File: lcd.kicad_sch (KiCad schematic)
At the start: 11 parts, among them J2 FPC-05F-12PH20, Q1 SS8050

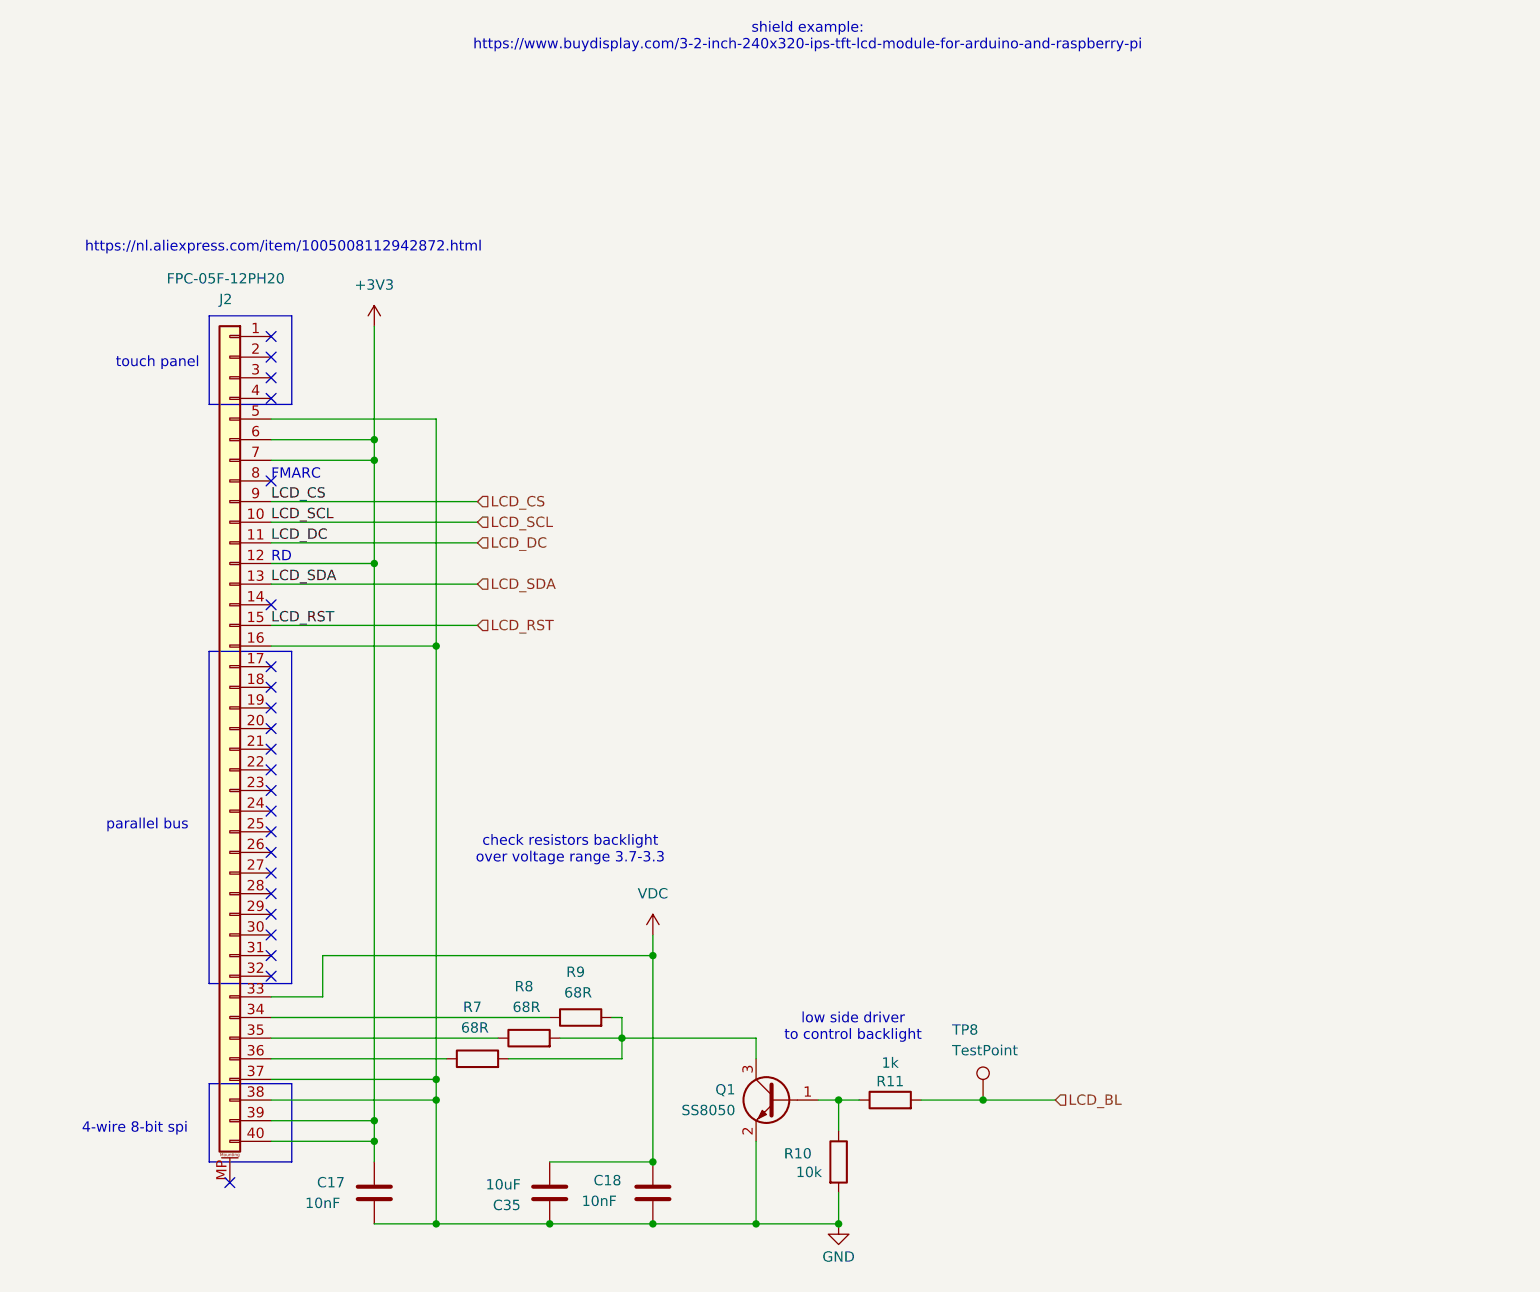
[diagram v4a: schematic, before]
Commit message: proper lcd backlight driver
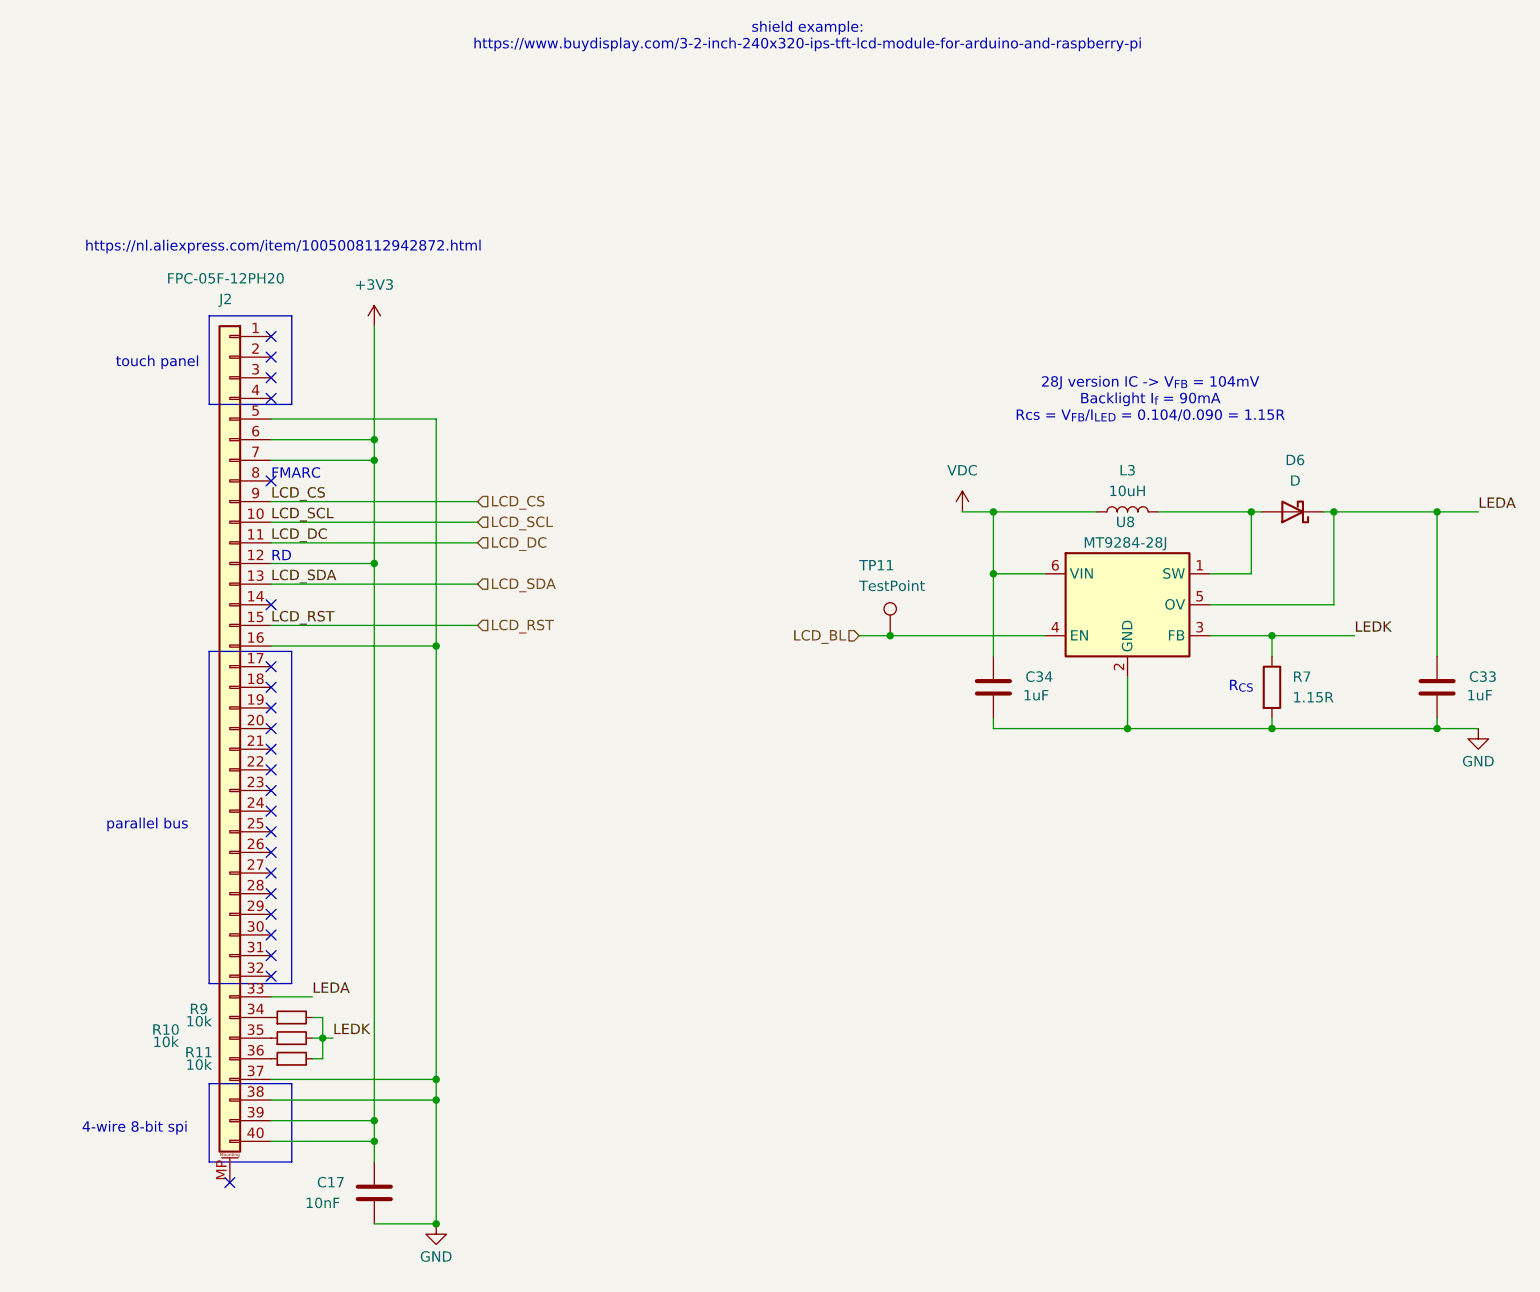
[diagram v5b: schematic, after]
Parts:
- removed C18: 10nF, Capacitor_SMD:C_0603_1608Metric, symbol Device:C
- removed C35: 10uF, Capacitor_SMD:C_0603_1608Metric, symbol Device:C
- removed Q1: SS8050, Package_TO_SOT_SMD:SOT-23, symbol Transistor_BJT:SS8050
- removed R10: 10k, Resistor_SMD:R_0603_1608Metric, symbol Device:R
- removed R11: 1k, Resistor_SMD:R_0402_1005Metric, symbol Device:R
- removed R8, R9: 68R, Resistor_SMD:R_0603_1608Metric, symbol Device:R
- removed TP8: TestPoint, TestPoint:TestPoint_Pad_D1.0mm, symbol Connector:TestPoint
- added C33, C34: 1uF, Capacitor_SMD:C_0402_1005Metric, symbol Device:C
- added D6: D, Diode_SMD:D_SMA, symbol Device:D_Schottky
- added L3: 10uH, Inductor_SMD:L_KOHERelec_MDA7030, symbol Device:L
- added R10, R11, R9: 10k, Resistor_SMD:R_0603_1608Metric, symbol Device:R_Small
- added TP11: TestPoint, TestPoint:TestPoint_Pad_D1.0mm, symbol Connector:TestPoint
- added U8: MT9284-28J, Package_TO_SOT_SMD:SOT-23-6, symbol MT9284-28J:MT9284
- R7: value 68R -> 1.15R; footprint Resistor_SMD:R_0603_1608Metric -> Resistor_SMD:R_0805_2012Metric; LCSC (none) -> C3016527
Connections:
- net GND: now also R7.2, C33.1, C34.1, U8.2 (GND)
- net LCD_BL: now also TP11.1, U8.4 (EN)
- net VDC: now also C34.2, L3.1, U8.6 (VIN); no longer J2.33 (Pin_33)
- net at J2.36 (Pin_36): now also R11.1; no longer R7.1
- net at J2.35 (Pin_35): now also R10.1
- net at J2.34 (Pin_34): now also R9.1
- new net: D6.2 (A), L3.2, U8.1 (SW)
- new net LEDA: C33.2, D6.1 (K), J2.33 (Pin_33), U8.5 (OV)
- new net LEDK: R10.2, R11.2, R7.1, R9.2, U8.3 (FB)
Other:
- note added: "28J version IC -> V_{FB} = 104mV Backlight I_{f} = 90mA Rcs = V_{FB}/I_{LED} = 0.104/0.090 = 1.15R"
- note added: "R_{CS}"
- note removed: "check resistors backlight over voltage range 3.7-3.3"
- note removed: "low side driver to control backlight"

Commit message: extra capacitance vibration, old backlight method
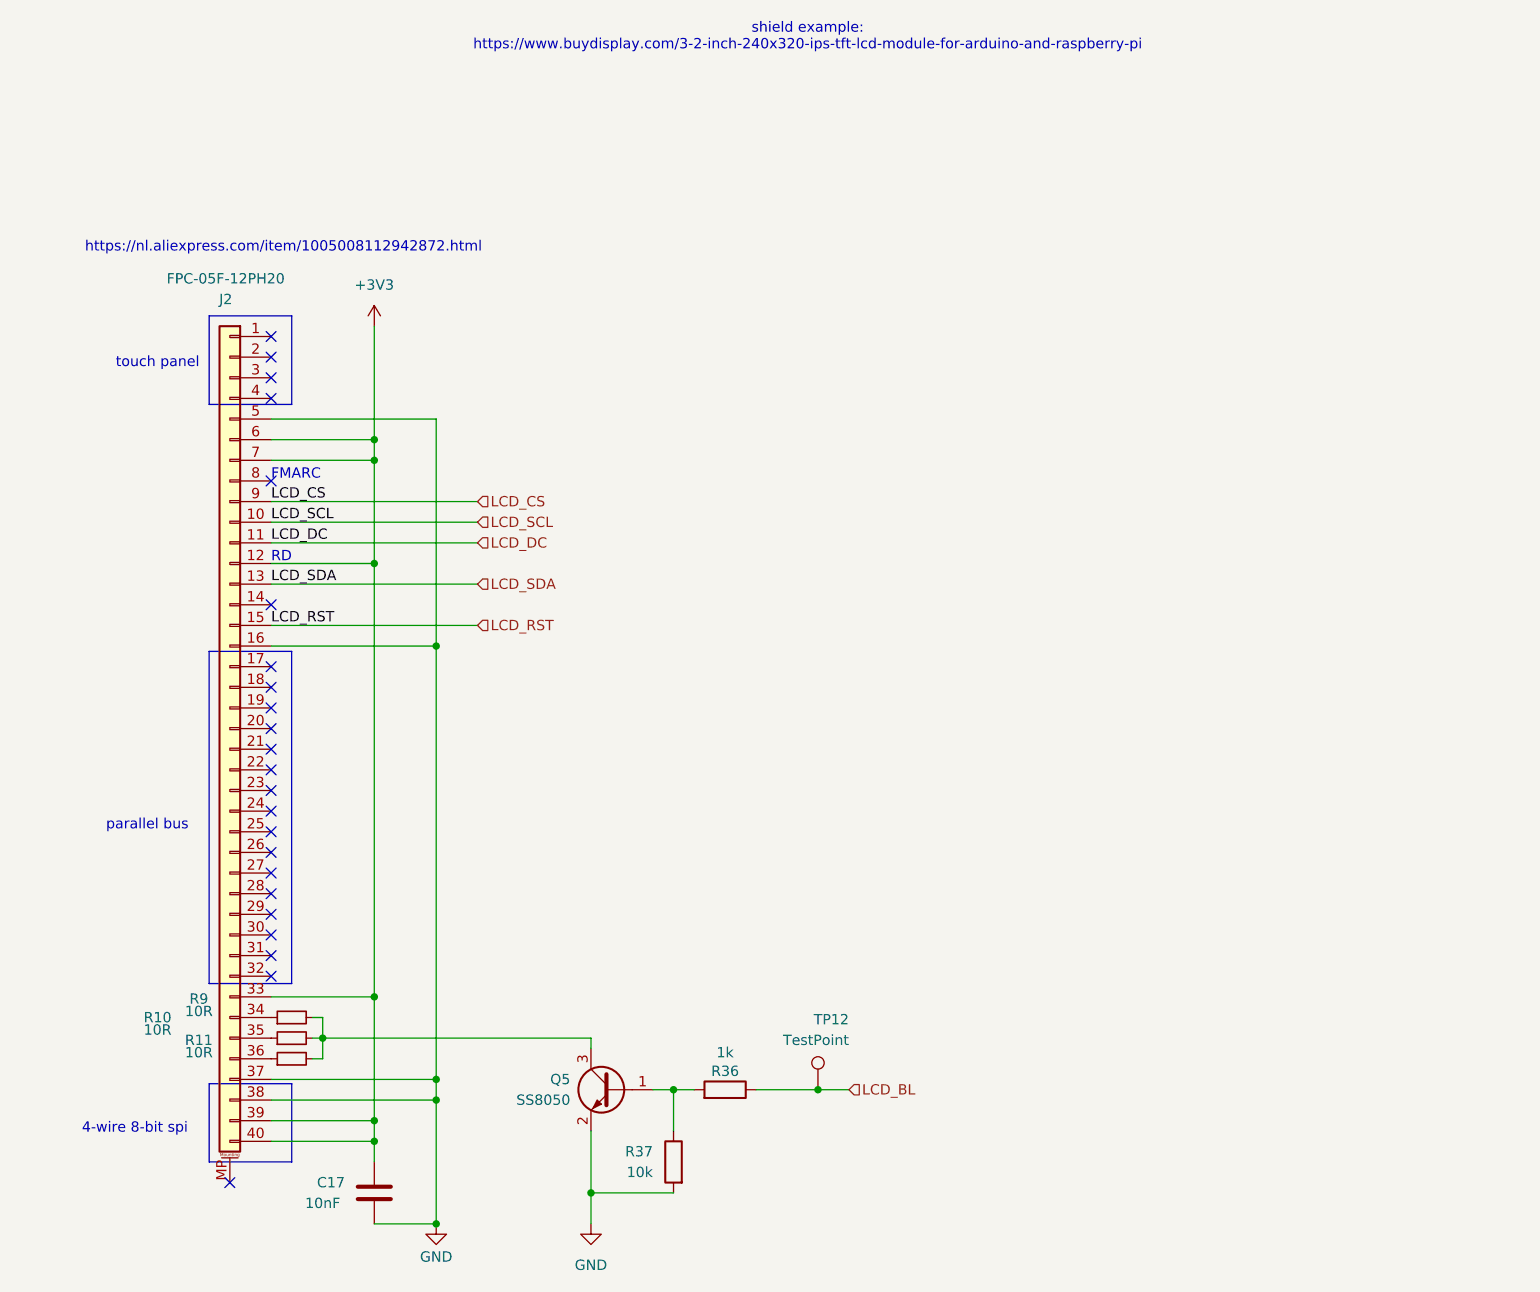
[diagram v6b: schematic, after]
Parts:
- removed C33, C34: 1uF, Capacitor_SMD:C_0402_1005Metric, symbol Device:C
- removed D6: D, Diode_SMD:D_SMA, symbol Device:D_Schottky
- removed L3: 10uH, Inductor_SMD:L_KOHERelec_MDA7030, symbol Device:L
- removed R7: 1.15R, Resistor_SMD:R_0805_2012Metric, symbol Device:R
- removed TP11: TestPoint, TestPoint:TestPoint_Pad_D1.0mm, symbol Connector:TestPoint
- removed U8: MT9284-28J, Package_TO_SOT_SMD:SOT-23-6, symbol MT9284-28J:MT9284
- added Q5: SS8050, Package_TO_SOT_SMD:SOT-23, symbol Transistor_BJT:SS8050
- added R36: 1k, Resistor_SMD:R_0603_1608Metric, symbol Device:R
- added R37: 10k, Resistor_SMD:R_0603_1608Metric, symbol Device:R
- added TP12: TestPoint, TestPoint:TestPoint_Pad_D1.0mm, symbol Connector:TestPoint
- R10, R11, R9: value 10k -> 10R; LCSC C109318 -> (none)
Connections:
- net LEDA is gone; now on net +3V3: J2.33 (Pin_33)
- net GND: now also Q5.2 (E), R37.2
- net LCD_BL: now also R36.1, TP12.1
- net LEDK: no longer names the net of R10.2, R11.2, R9.2
- net LEDK: now also Q5.3 (C)
- new net: Q5.1 (B), R36.2, R37.1
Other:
- note removed: "28J version IC -> V_{FB} = 104mV Backlight I_{f} = 90mA Rcs = V_{FB}/I_{LED} = 0.104/0.090 = 1.15R"
- note removed: "R_{CS}"

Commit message: changes for production
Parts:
- C17: LCSC C36508 -> (none); Manufacturer FH -> (none); Manufacturer Part Number 0603CG8R0C500NT -> (none)
- J2: value FPC-05F-12PH20 -> FPC-05F-40PH20; LCSC C2856799 -> C2856812; Manufacturer Part Number FPC-05F-12PH20 -> FPC-05F-40PH20
- TP12: now left out of the parts list
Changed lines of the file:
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@@
 			)
 		)
-		(property "LCSC" "C36508"
+		(property "LCSC" ""
 			(at 87.63 165.1 0)
 			(effects
@@
 			)
 		)
-		(property "Manufacturer" "FH"
+		(property "Manufacturer" ""
 			(at 87.63 165.1 0)
 			(effects
@@
 			)
 		)
-		(property "Manufacturer Part Number" "0603CG8R0C500NT"
+		(property "Manufacturer Part Number" ""
 			(at 87.63 165.1 0)
 			(effects
@@
 			)
 		)
-		(property "Value" "FPC-05F-12PH20"
+		(property "Value" "FPC-05F-40PH20"
 			(at 69.342 52.578 0)
 			(effects
@@
 			)
 		)
-		(property "LCSC" "C2856799"
+		(property "LCSC" "C2856812"
 			(at 69.85 107.95 0)
 			(effects
@@
 			)
 		)
-		(property "Manufacturer Part Number" "FPC-05F-12PH20"
+		(property "Manufacturer Part Number" "FPC-05F-40PH20"
 			(at 69.85 107.95 0)
 			(effects
@@
 		(unit 1)
 		(exclude_from_sim no)
-		(in_bom yes)
-		(on_board yes)
-		(dnp no)
+		(in_bom no)
+		(on_board yes)
+		(dnp no)

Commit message: align some components with inventory
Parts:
- C17: footprint Capacitor_SMD:C_0603_1608Metric -> Capacitor_SMD:C_0402_1005Metric
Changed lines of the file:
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@@
 			)
 		)
-		(property "Footprint" "Capacitor_SMD:C_0603_1608Metric"
+		(property "Footprint" "Capacitor_SMD:C_0402_1005Metric"
 			(at 86.6648 161.29 0)
 			(effects
